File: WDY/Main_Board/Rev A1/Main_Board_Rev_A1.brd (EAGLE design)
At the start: 130 x 70 mm, 193 parts, among them J1 22-05-7028-02, J10 22-05-7038-03, J11 22-05-7028-02, J12 22-05-7028-02, J13 22-05-7028-02, J14 22-05-7028-02, J15 22-05-7058-05, J16 22-27-2061-06, J2 22-05-7028-02, J3 22-05-7048-04, J4 22-05-7048-04, J5 1241050-5, J6 90814-0208, J7 90814-0206, J8 90814-0208, J9 22-05-7038-03, K1 G6K-2G-Y, K2 G6K-2G-Y, K3 G6K-2G-Y, K4 G6K-2G-Y, P1 RB1-125BAG1A, SW1 B3FS-1015, SW2 B3FS-1015, T1 MMBT2222AL, U1 LPC1768FBD100, U11 SN74LVC3G17DCTR, U2 SN74LVC3G17DCTR, U3 SN74LVC3G17DCTR, U4 TPL0401A, U5 AT24C512C-SSHM-B, U6 SN74LVC2G17DBVR, U7 SN74LVC2G17DBVR, U8 LT1767EMS8E-5PBF, U9 TC1264-3.3, X1 FC-135, X2 MSTBA2

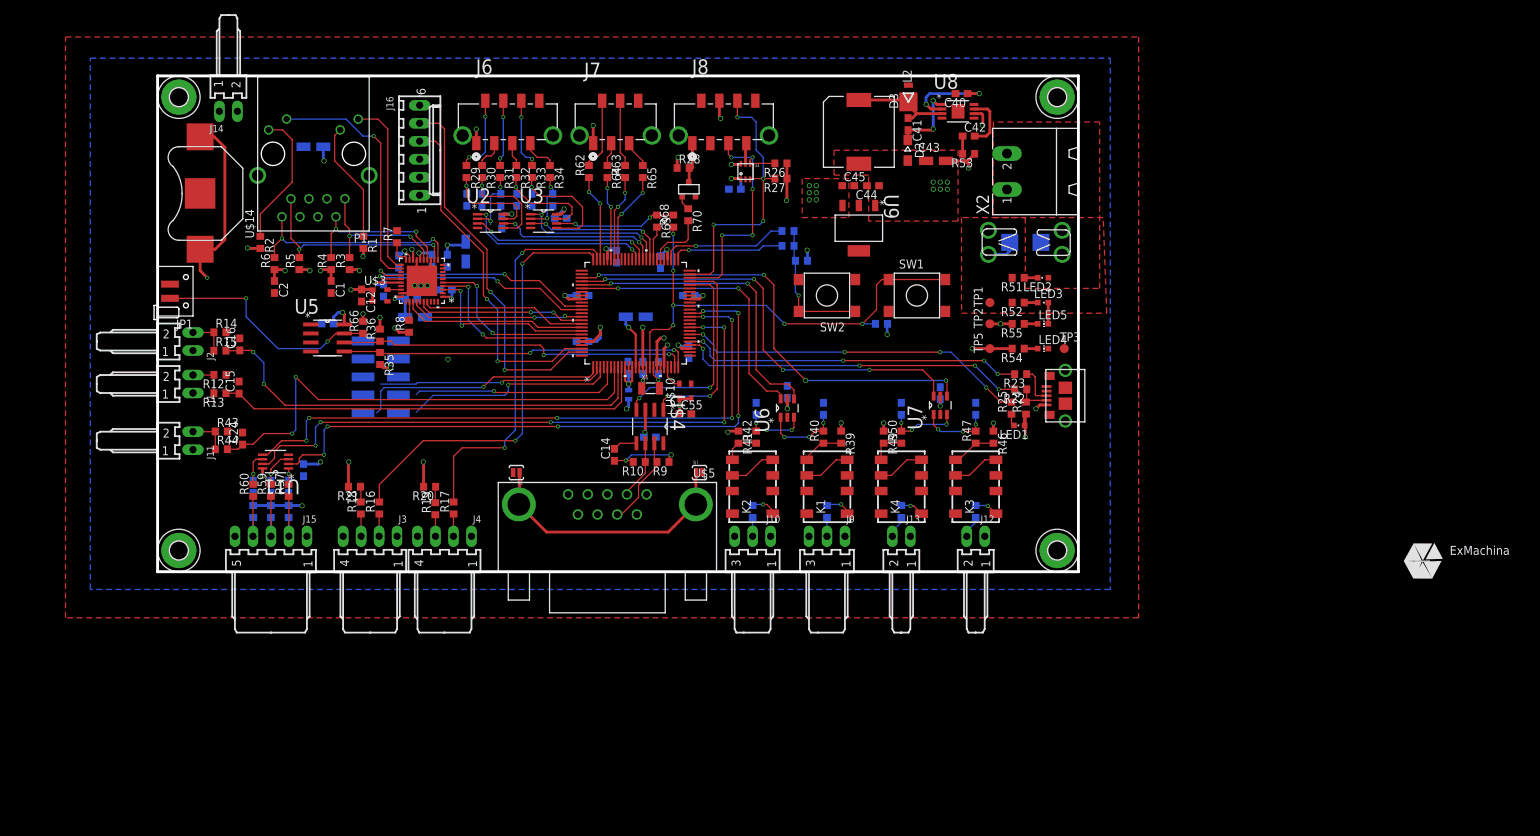
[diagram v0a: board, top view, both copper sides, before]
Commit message: Rename board to Main_Board_Rev_A1
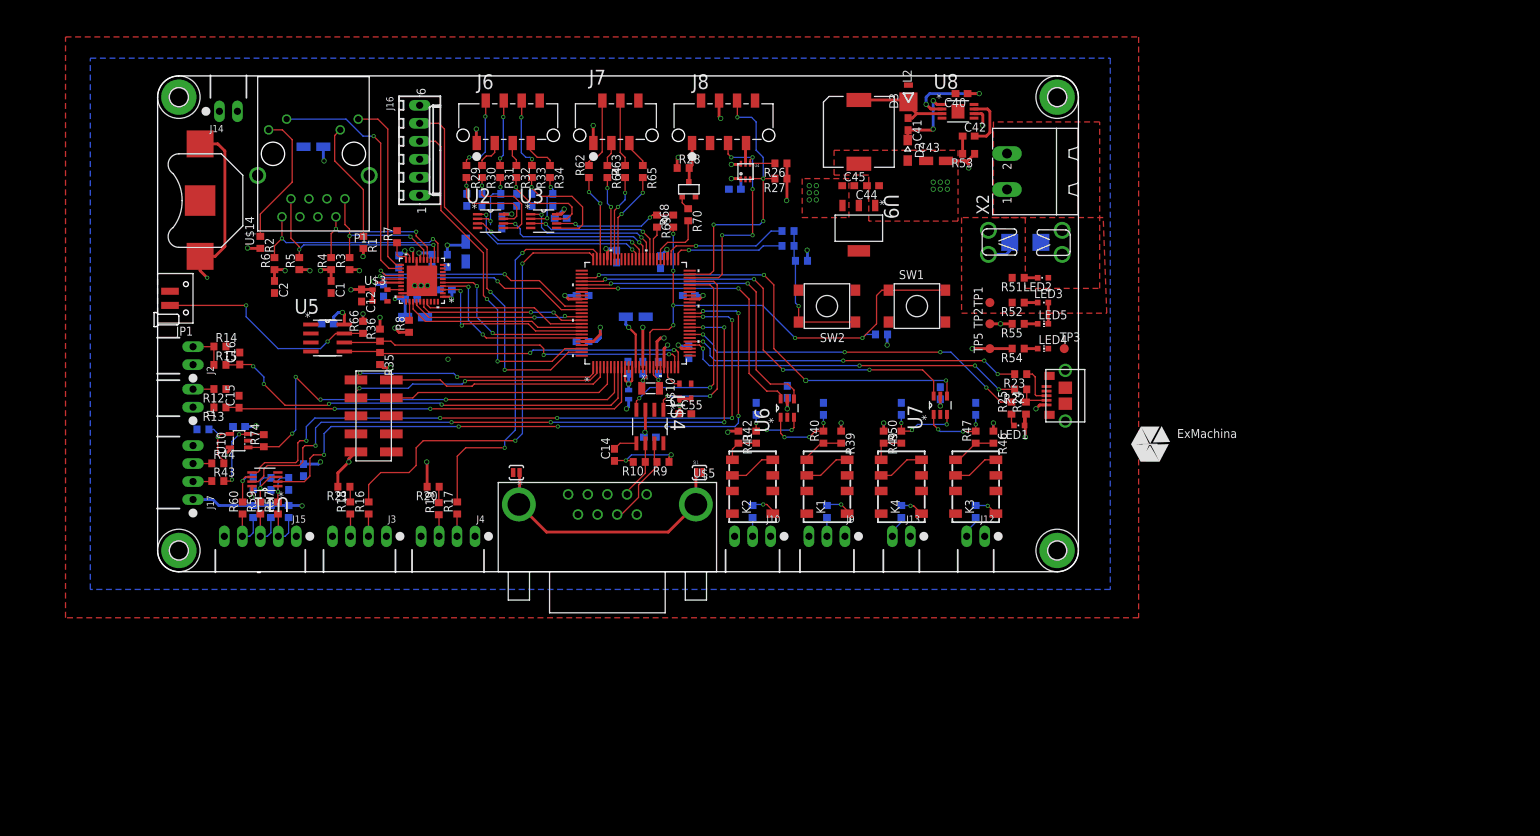
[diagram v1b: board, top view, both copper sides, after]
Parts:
- removed J11: 22-05-7028-02, con-molex:7395-02
- added J17: 22-05-7048-04, con-molex:7395-04
- added R73, R74: 1k2, rcl:R0603
- added U10: TLV313, ti:SOT23-DBV
- C24: value 4.7uF -> 0.1uF
- R43, R44: value 10k -> 1k8
- moved U$9 231.5 mm to (163.0, 41.5)
- moved U$1 41.9 mm to (140.1, 18.0)
- moved R43 7.02 mm to (8.50, 12.8)
- moved J5 5.59 mm to (30.5, 22.0), flipped to the top, turned to 90 degrees
- moved J6 5.52 mm to (49.5, 63.7)
- moved J8 5.44 mm to (79.9, 63.7)
- moved J7 4.53 mm to (64.7, 63.7)
- moved R57 2.92 mm to (17.0, 9.00)
- moved R59 2.92 mm to (14.5, 9.00)
- moved R60 2.92 mm to (12.0, 9.00)
- moved U11 2.92 mm to (15.2, 13.1)
- moved R44 2.06 mm to (8.50, 15.3)
- moved C15 2.00 mm to (11.5, 24.0)
- moved C16 2.00 mm to (11.6, 30.1)
- moved J1 2.00 mm to (5.00, 24.5)
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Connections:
- new net N$31: J17.2, R43.1
- new net N$61: R43.2, R74.2, U10.3
- new net N$68: J17.3, R44.1
- net +3V3: now also C24.1, U10.5
- net +5V: now also J17.1
- net ADC_SLACK_DETECTION: now also R74.1, U10.1; no longer C24.1, R44.2
- net AVDD: no longer J11.1
- net GND: now also J17.4, R73.1, U10.2; no longer R43.2
- net N$67: now also R44.2, R73.2, U10.4; no longer J11.2, R43.1, R44.1
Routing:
- net N$61: track 0.00 -> 11.6 mm, vias 0 -> 2
- net +5V: track 113.0 -> 121.9 mm
- net +3V3: track 152.8 -> 158.7 mm, vias 49 -> 51
- net JTAG_TDI: track 33.0 -> 36.8 mm, vias 1 -> 2
- net ENCODER_B: track 90.1 -> 93.8 mm
- net ENCODER_A: track 88.0 -> 91.7 mm
- net JTAG_TCK: track 30.2 -> 33.7 mm, vias 1 -> 0
- net ENCODER_Z: track 90.9 -> 94.3 mm
- net ADC_SLACK_DETECTION: track 68.6 -> 65.5 mm, vias 2 -> 4
- net FAN_1_PWM: track 60.8 -> 63.8 mm
- net N$31: track 0.00 -> 2.68 mm
- net N$68: track 0.00 -> 2.66 mm
- net N$54: track 3.21 -> 5.51 mm
- net N$67: track 5.68 -> 7.94 mm, vias 0 -> 1
- net ADC_TEMP_1: track 65.1 -> 63.4 mm, vias 2 -> 4
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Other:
- outline, holes or cut-outs redrawn

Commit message: Update libraries
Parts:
- moved J10 1.50 mm to (85.5, 5.00)
- moved J12 1.50 mm to (117.0, 5.00)
- moved J13 1.50 mm to (106.5, 5.00)
- moved J9 1.50 mm to (96.0, 5.00)
- moved K1 1.50 mm to (96.0, 12.0)
- moved K2 1.50 mm to (85.5, 12.0)
- moved K3 1.50 mm to (117.0, 12.0)
- moved K4 1.50 mm to (106.5, 12.0)
- moved C15 1.00 mm to (11.5, 23.0)
- moved J1 1.00 mm to (5.00, 23.5)
- moved R12 1.00 mm to (8.80, 24.8)
- moved R13 1.00 mm to (8.80, 22.2)
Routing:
- net N$33: track 3.33 -> 4.83 mm
- net N$28: track 3.33 -> 4.83 mm
- net N$55: track 3.71 -> 5.16 mm
- net N$24: track 3.71 -> 5.16 mm
- net N$37: track 3.18 -> 4.16 mm
- net N$32: track 3.18 -> 4.16 mm
- net N$34: track 6.32 -> 5.41 mm
- net N$36: track 4.99 -> 5.82 mm
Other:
- board text added: "ENCODER"
- board text added: "FAN 1"
- board text added: "FAN 2"
- board text added: "SLACK"
- board text added: "TEMP_0"
- board text added: "TEMP_1"

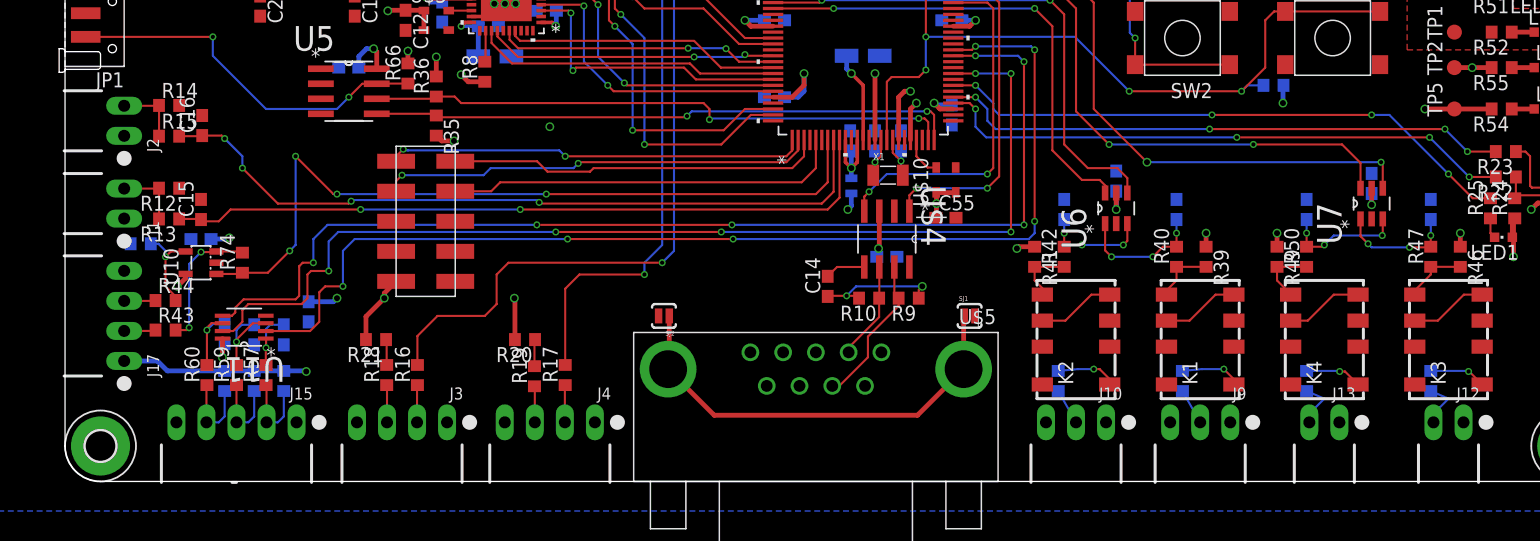
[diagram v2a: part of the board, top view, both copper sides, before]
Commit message: Add Cortex M debug connector
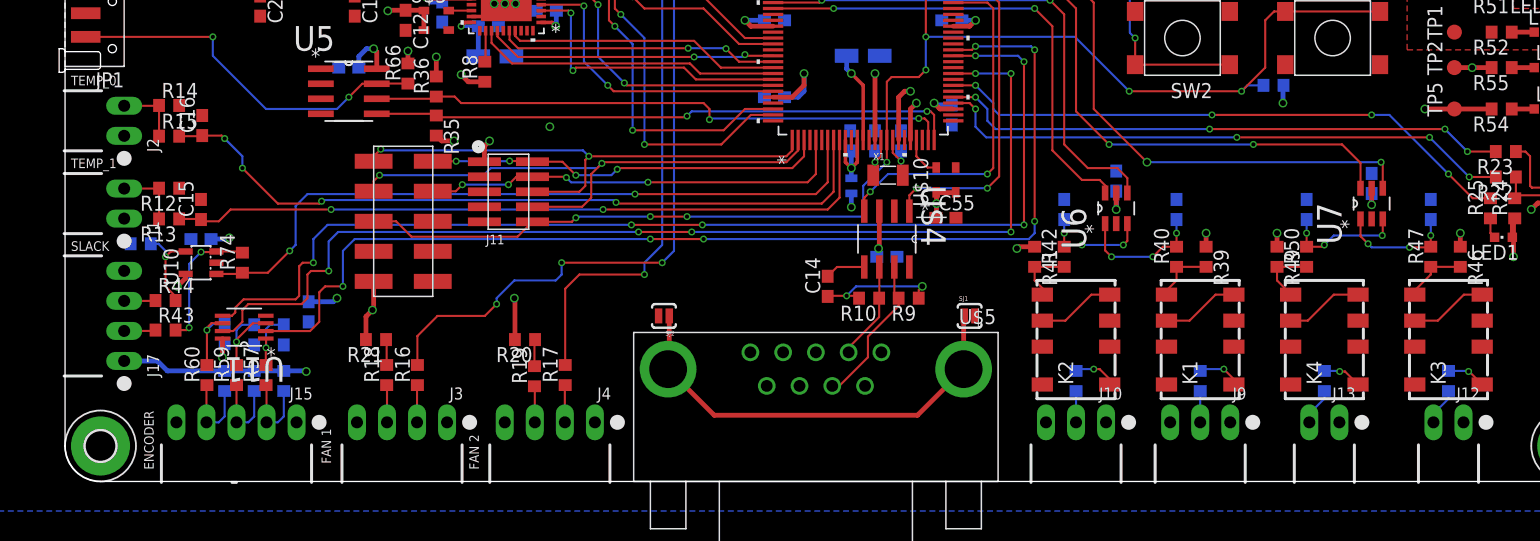
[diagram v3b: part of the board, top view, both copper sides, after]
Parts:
- added J11: FTSH-105-01-L-DV, con-samtec:FTSH-105-01-L-DV
- moved J5 1.90 mm to (28.6, 22.0)
- moved R37 1.50 mm to (85.5, 8.50)
- moved R38 1.50 mm to (96.0, 8.50)
- moved R45 1.50 mm to (117.0, 8.50)
- moved R48 1.50 mm to (106.5, 8.50)
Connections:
- removed net JTAG_RST: J5.5
- net +3V3: now also J11.1
- net GND: now also J11.3, J11.5, J11.9
- net JTAG_TCK: now also J11.4
- net JTAG_TDI: now also J11.8
- net JTAG_TDO: now also J11.6
- net JTAG_TMS: now also J11.2
- net RESET: now also J11.10, J5.5
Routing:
- net RESET: track 70.6 -> 120.5 mm, vias 6 -> 10
- net JTAG_TDI: track 36.8 -> 47.3 mm
- net JTAG_TDO: track 35.5 -> 44.7 mm
- net ADC_SLACK_DETECTION: track 65.5 -> 60.4 mm, vias 4 -> 2
- net JTAG_TCK: track 33.7 -> 36.3 mm, vias 0 -> 4
- net JTAG_TMS: track 31.8 -> 33.9 mm, vias 0 -> 4
- net N$33: track 4.83 -> 3.33 mm
- net N$28: track 4.83 -> 3.33 mm
- net N$55: track 5.16 -> 3.71 mm
- net N$24: track 5.16 -> 3.71 mm
- net N$37: track 4.16 -> 3.18 mm
- net N$32: track 4.16 -> 3.18 mm
- net +3V3: track 158.7 -> 159.5 mm, vias 51 -> 52
- net FAN_1_PWM: track 63.8 -> 63.2 mm, vias 2 -> 4

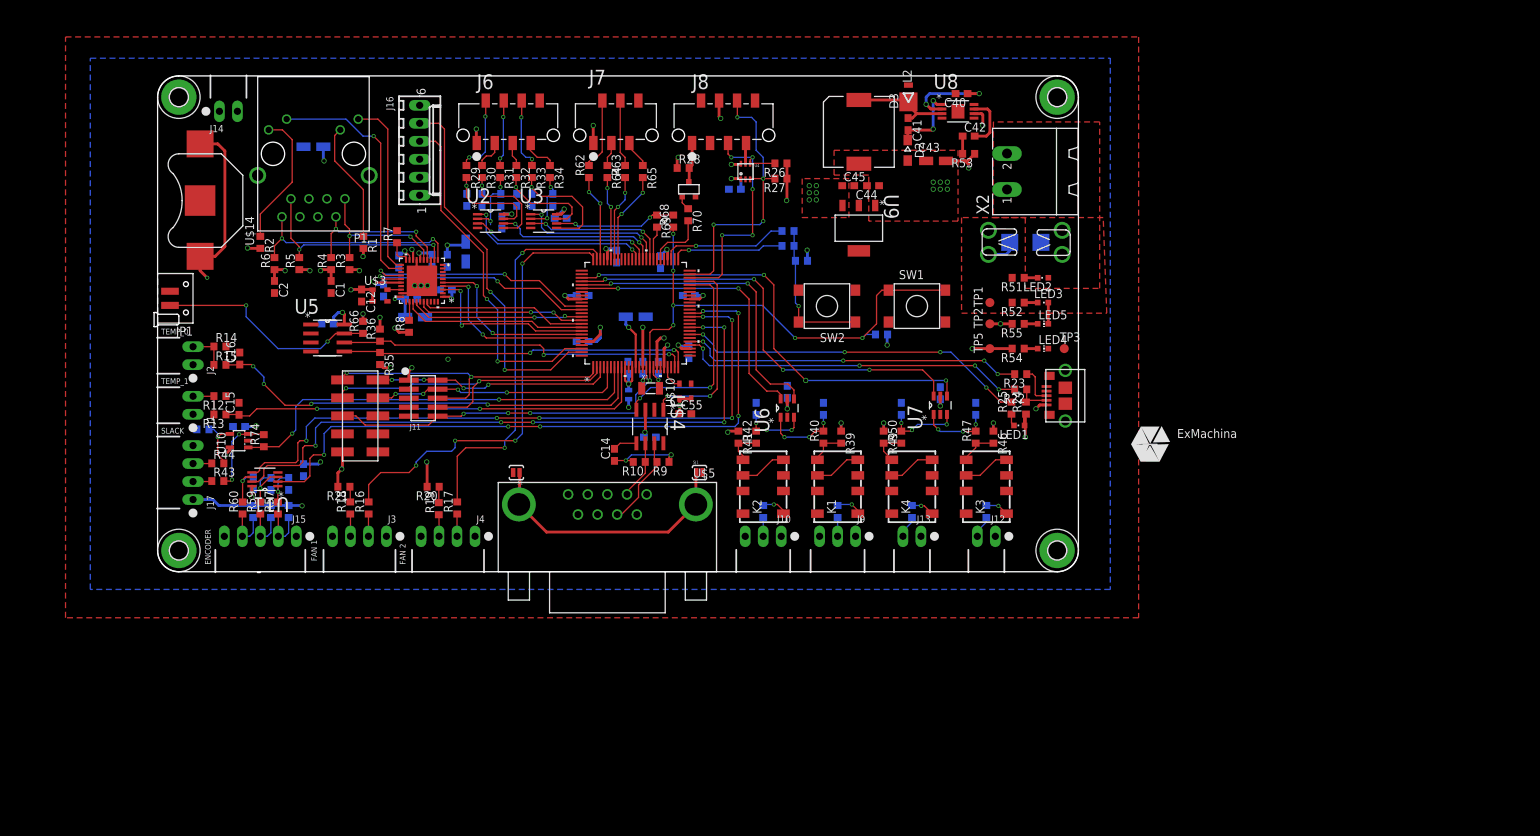
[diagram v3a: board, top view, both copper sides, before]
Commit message: Add name and fiducial
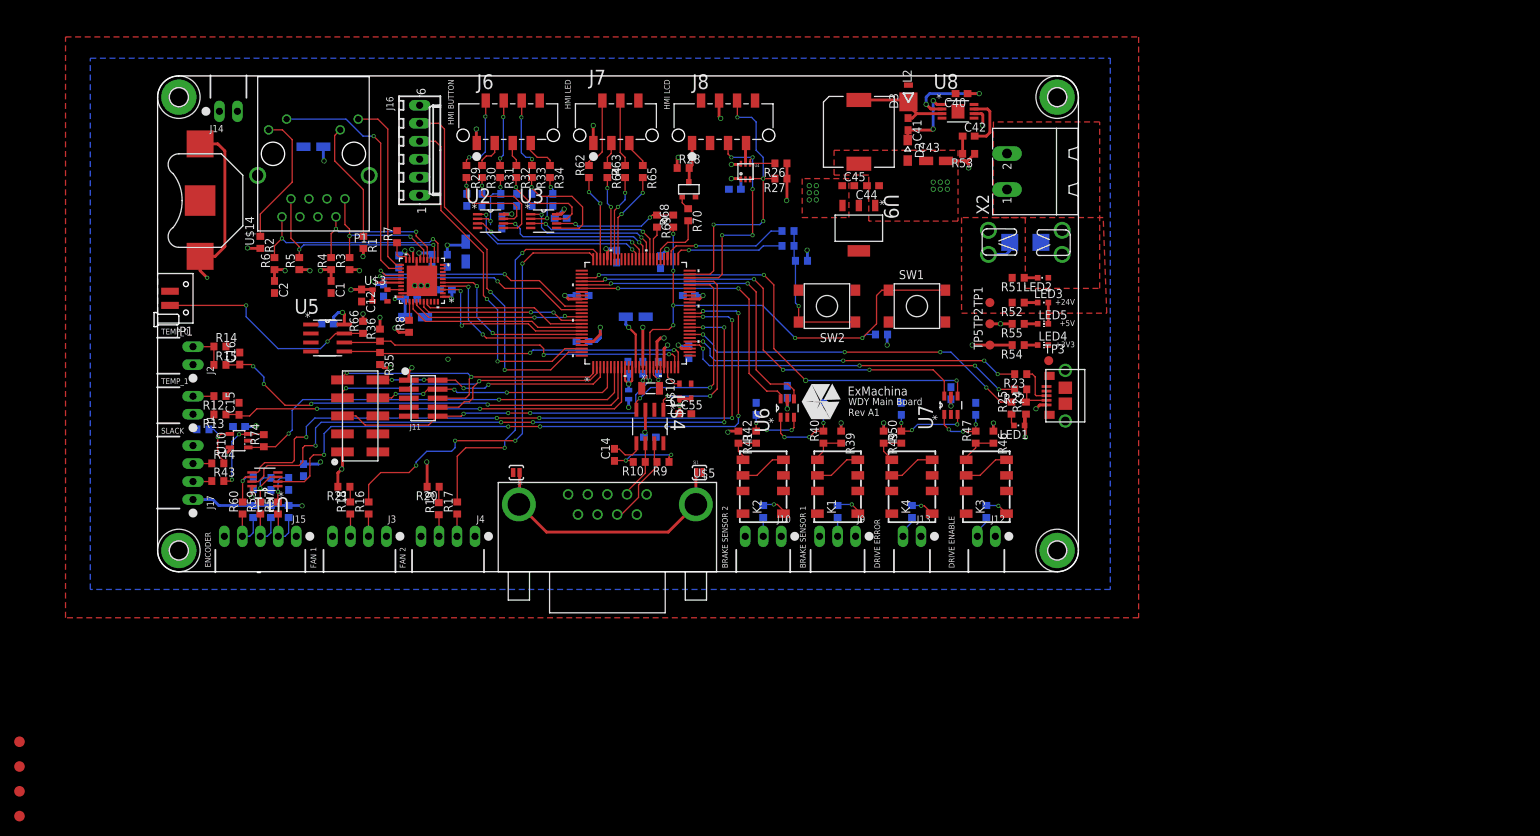
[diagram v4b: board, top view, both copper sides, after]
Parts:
- removed U$9: (no value), frames:A4L-LOC
- added JP2, JP3, JP4, JP5: FIDUCIAL1.5X3, SparkFun:FIDUCIAL-1.5X3
- moved U$1 46.9 mm to (93.6, 24.0)
- moved TP3 2.78 mm to (125.8, 29.8)
- moved C52 1.50 mm to (112.0, 25.2)
- moved U7 1.50 mm to (112.0, 23.5)
- moved LED4 0.50 mm to (125.0, 32.0)
- moved R54 0.50 mm to (121.5, 32.0)
- moved TP5 0.50 mm to (117.5, 32.0)
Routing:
- net N$42: track 10.5 -> 12.0 mm
- net N$41: track 10.1 -> 8.61 mm
- net DRIVE_ERR: track 65.3 -> 66.8 mm
- net DRIVE_EN: track 63.0 -> 64.5 mm
- net +3V3: track 159.5 -> 158.0 mm
- net CAN_SPLIT: track 3.42 -> 4.74 mm
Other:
- board text added: "+24V"
- board text added: "+3V3"
- board text added: "+5V"
- board text added: "BRAKE SENSOR 1"
- board text added: "BRAKE SENSOR 2"
- board text added: "DRIVE ENABLE"
- board text added: "DRIVE ERROR"
- board text added: "HMI BUTTON"
- board text added: "HMI LCD"
- board text added: "HMI LED"
- board text added: "WDY Main Board Rev A1"
